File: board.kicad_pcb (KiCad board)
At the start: 2 copper layers, 96.3 x 46.3 mm, 38 parts, among them J0 Battery Pads, J1 PGRM, J2 Micro SD Slot, J3 USB_B_Micro, SW0 RESET, SW1 UP, SW2 DOWN, SW3 LEFT, SW4 RIGHT, SW5 BTN_A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

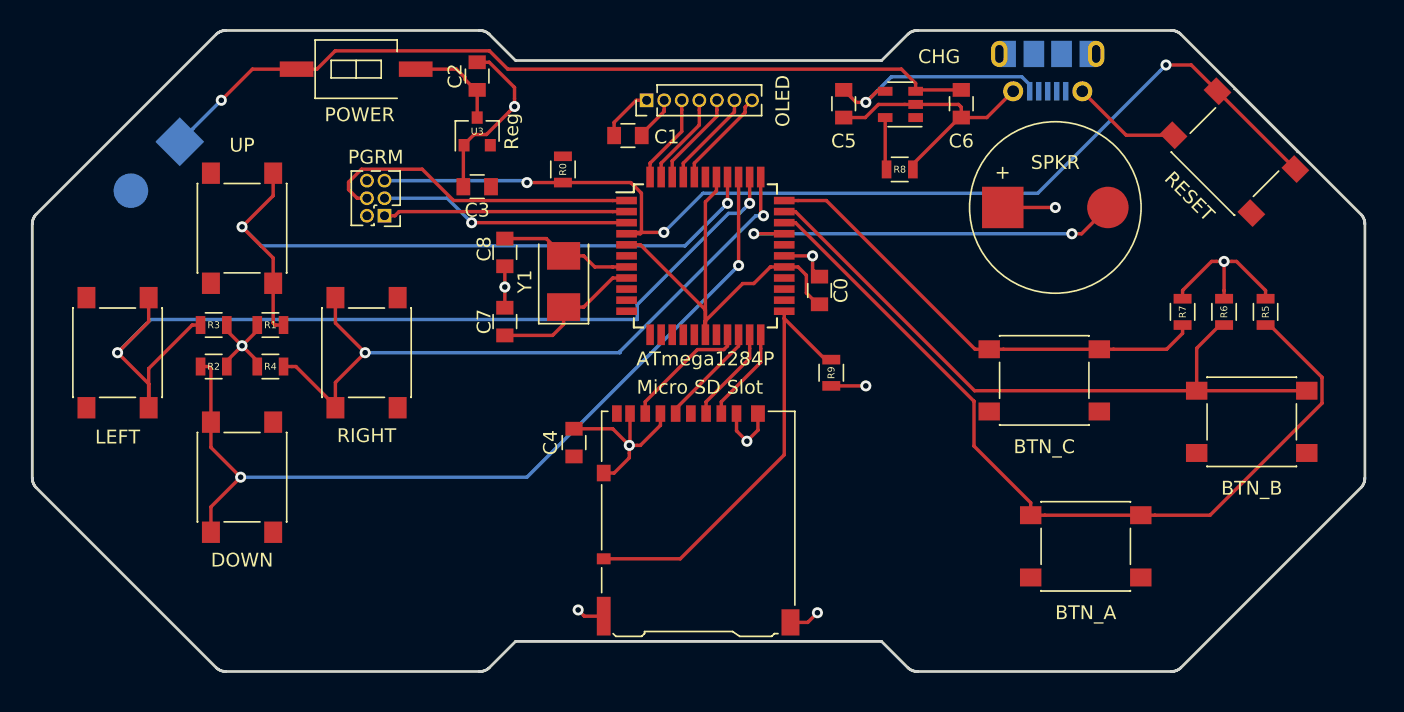
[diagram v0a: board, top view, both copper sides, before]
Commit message: reworked to be MCU agnostic
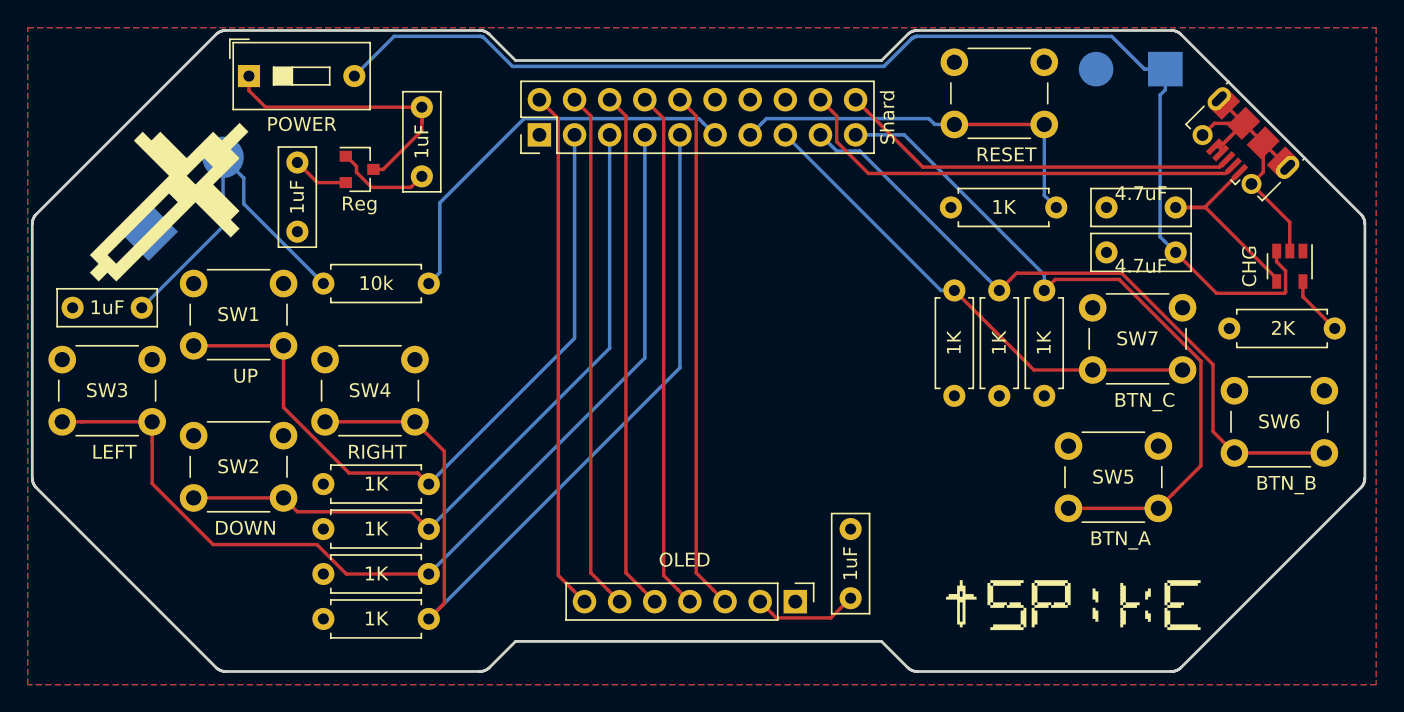
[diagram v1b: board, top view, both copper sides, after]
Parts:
- removed C0: 1uF, Capacitors_SMD:C_0805
- removed C7, C8: 22pF, Capacitors_SMD:C_0805
- removed J3: USB_B_Micro, Connectors_USB:USB_Micro-B_Molex-105017-0001
- removed U0: ATmega1284P, Housings_QFP:TQFP-44_10x10mm_Pitch0.8mm
- removed Y1: 16MHz, Crystals:Crystal_SMD_5032-2pin_5.0x3.2mm
- added LOGO: , LOGO, F.Cu at (168.5, 122.2)
- added SPIKE: , SPIKE, F.Cu at (114.0, 84.3)
- C1, C2, C3, C4, C5, C6: footprint Capacitors_SMD:C_0805 -> Capacitor_THT:C_Rect_L7.0mm_W2.5mm_P5.00mm
- J1: value PGRM -> Shard; footprint Pin_Headers:Pin_Header_Straight_2x03_Pitch1.27mm -> Connector_PinHeader_2.54mm:PinHeader_2x10_P2.54mm_Vertical
- J2: value Micro SD Slot -> USB-Micro; footprint Connectors_Card:Hirose_DM3AT-SF-PEJM5 -> Connector_USB:USB_Micro-B_Molex-105017-0001
- LS1: moved to B.Cu
- R0, R1, R2, R3, R4, R5, R6, R7, R8: footprint Resistors_SMD:R_0805 -> Resistor_THT:R_Axial_DIN0207_L6.3mm_D2.5mm_P7.62mm_Horizontal
- R9: value 1K -> 10k; footprint Resistors_SMD:R_0805 -> Resistor_THT:R_Axial_DIN0207_L6.3mm_D2.5mm_P7.62mm_Horizontal
- SW0, SW1, SW2, SW3, SW4, SW5, SW6, SW7: footprint Buttons_Switches_SMD:SW_SPST_PTS645 -> Button_Switch_THT:SW_PUSH_6mm
- SW8: footprint Buttons_Switches_SMD:SW_DIP_x1_W8.61mm_Slide_LowProfile -> Button_Switch_THT:SW_DIP_SPSTx01_Slide_9.78x4.72mm_W7.62mm_P2.54mm
- U1: footprint Custom Footprints:128x128_OLED -> Custom Footprints:128x128-OLED
- U2: footprint TO_SOT_Packages_SMD:SOT-23-5 -> Package_TO_SOT_SMD:SOT-23-5
- U3: footprint TO_SOT_Packages_SMD:SOT-23 -> Package_TO_SOT_SMD:SOT-23
- moved J0 65.2 mm to (182.2, 85.5), turned to 180 degrees
- moved LS1 61.8 mm to (111.2, 97.2), turned to 45 degrees
- moved J2 41.6 mm to (190.2, 91.0), turned to 135 degrees
- moved U1 37.8 mm to (158.0, 124.0), turned to 270 degrees
- moved C1 37.1 mm to (162.0, 123.8), turned to 90 degrees
- moved R8 33.5 mm to (197.0, 104.2), turned to 180 degrees
- moved C4 32.7 mm to (110.8, 102.8), turned to 180 degrees
- moved U2 30.5 mm to (193.8, 99.8), turned to 270 degrees
- moved R9 29.8 mm to (131.5, 101.0), turned to 180 degrees
- moved R0 28.2 mm to (169.2, 95.5), turned to 0 degrees
- moved C5 25.1 mm to (185.5, 95.5), turned to 180 degrees
- moved R3 23.8 mm to (131.5, 122.0), turned to 180 degrees
- moved R4 21.5 mm to (131.5, 125.2)
- moved SW0 21.3 mm to (169.5, 85.0), turned to 0 degrees
- moved R2 19.5 mm to (131.5, 118.8), turned to 180 degrees
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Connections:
- C4 pad 1: +3V3 -> Net-(C4-Pad1)
- J1 pad 1: MISO -> +3V3
- J1 pad 2: +3V3 -> D_CS
- J1 pad 3: SCK -> UP
- J1 pad 4: MOSI -> D_DC
- J1 pad 5: RESET -> DOWN
- J1 pad 6: GND -> D_RST
- J2 pad 1: GND -> CHARGE
- J2 pad 2: SD_CS -> D-
- J2 pad 3: SD_MOSI -> D+
- J2 pad 4: +3V3 -> GND
- J2 pad 5: SD_SCK -> GND
- LS1 pad 2: SND -> Net-(C4-Pad1)
- R9 pad 1: SD_DETECT -> SND
- R9 pad 2: GND -> Net-(C4-Pad1)
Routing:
- net GND: track 99.3 -> 31.7 mm, vias 11 -> 0
- net RESET: track 79.4 -> 28.3 mm, vias 3 -> 0
- net D-: track 0.00 -> 33.4 mm
- net SD_DETECT: track 31.2 -> 0.00 mm
- net D_SCK: track 6.50 -> 37.6 mm
- net D_MOSI: track 6.69 -> 37.6 mm
- net D_RST: track 6.89 -> 37.6 mm
- net D_DC: track 7.08 -> 37.6 mm
- net D_CS: track 7.28 -> 37.6 mm
- net D+: track 0.00 -> 29.1 mm
- net +BATT: track 60.8 -> 88.9 mm, vias 1 -> 0
- net Net-(C4-Pad1): track 0.00 -> 25.4 mm
- net +3V3: track 37.1 -> 11.7 mm
- net MOSI: track 23.6 -> 0.00 mm
- net SCK: track 18.2 -> 0.00 mm, vias 1 -> 0
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- added copper zone on F.Cu, net +3V3
- added copper zone on B.Cu, net GND

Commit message: added mounting holes
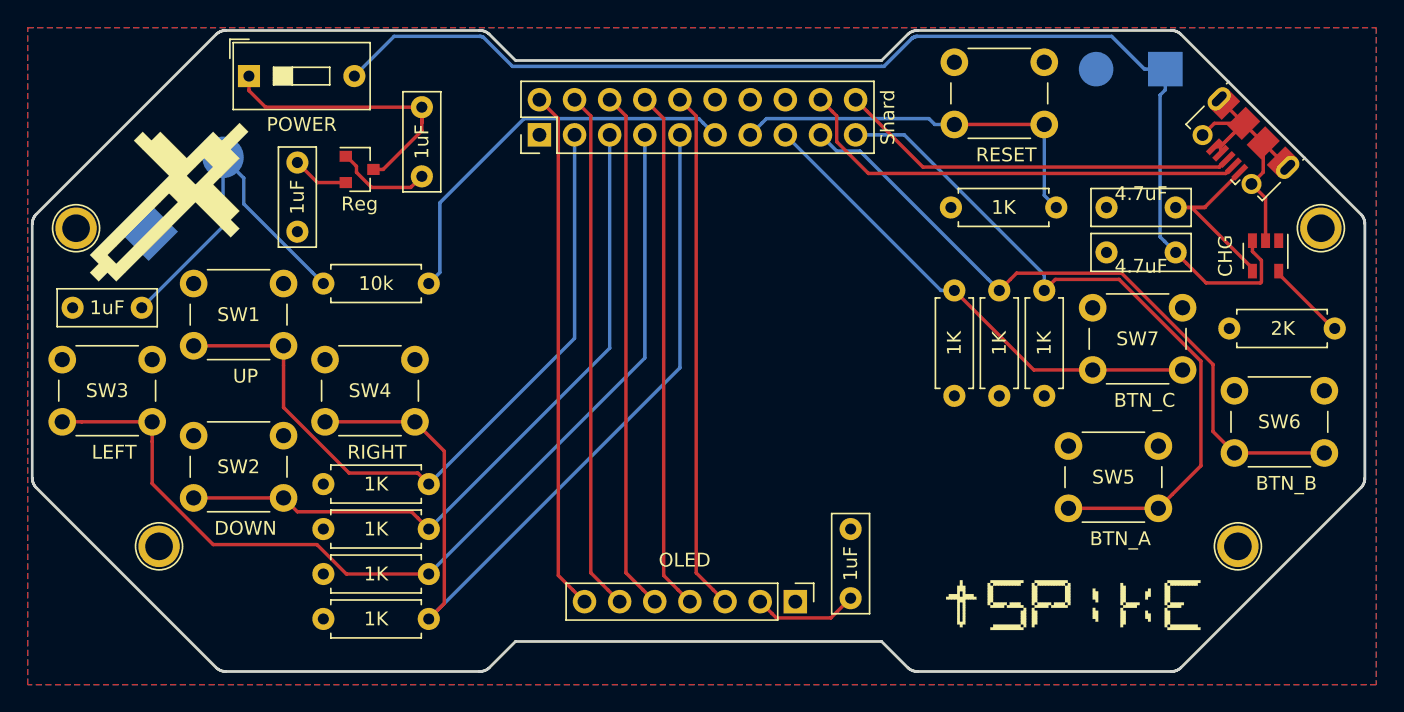
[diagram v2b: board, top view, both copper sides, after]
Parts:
- added REF**: TestPoint_Plated_Hole_D2.0mm, TestPoint:TestPoint_Plated_Hole_D2.0mm, F.Cu at (196.0, 97.0)
- added REF**: TestPoint_Plated_Hole_D2.0mm, TestPoint:TestPoint_Plated_Hole_D2.0mm, F.Cu at (106.0, 97.0)
- added REF**: TestPoint_Plated_Hole_D2.0mm, TestPoint:TestPoint_Plated_Hole_D2.0mm, F.Cu at (190.0, 120.0)
- added REF**: TestPoint_Plated_Hole_D2.0mm, TestPoint:TestPoint_Plated_Hole_D2.0mm, F.Cu at (112.0, 120.0)
- moved U2 1.90 mm to (192.0, 99.0)
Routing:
- net +BATT: track 88.9 -> 86.8 mm
- net Net-(R8-Pad1): track 4.35 -> 5.89 mm
- net GND: track 31.7 -> 30.2 mm
- net CHARGE: track 15.3 -> 14.3 mm
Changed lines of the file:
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@@
     (thickness 1.6)
     (drawings 102)
-    (tracks 182)
+    (tracks 185)
     (zones 0)
-    (modules 34)
+    (modules 38)
     (nets 25)
   )
@@
     (32 B.Adhes user hide)
     (33 F.Adhes user hide)
-    (34 B.Paste user)
+    (34 B.Paste user hide)
     (35 F.Paste user hide)
     (36 B.SilkS user)
@@
     (44 Edge.Cuts user)
     (45 Margin user hide)
-    (46 B.CrtYd user)
-    (47 F.CrtYd user)
-    (48 B.Fab user)
+    (46 B.CrtYd user hide)
+    (47 F.CrtYd user hide)
+    (48 B.Fab user hide)
     (49 F.Fab user hide)
   )
@@
       (outputformat 1)
       (mirror false)
-      (drillshape 1)
+      (drillshape 0)
       (scaleselection 1)
-      (outputdirectory ""))
+      (outputdirectory "/Users/mikewatts/Desktop/spike_gerbers/"))
   )
   (net 0 "")
@@
     (add_net SND)
     (add_net UP)
+  )
+  (module TestPoint:TestPoint_Plated_Hole_D2.0mm (layer F.Cu)
+    (at 196 97)
+    (descr "Plated Hole as test Point, diameter 2.0mm")
+    (tags "test point plated hole")
+    (attr virtual)
+    (fp_text reference REF** (at 0 -2.498) (layer F.Fab)
+      (effects (font (size 1 1) (thickness 0.15)))
+    )
+    (fp_text value TestPoint_Plated_Hole_D2.0mm (at 0 2.45) (layer F.Fab)
+      (effects (font (size 1 1) (thickness 0.15)))
+    )
+    (fp_text user %R (at 0 -2.5) (layer F.Fab)
+      (effects (font (size 1 1) (thickness 0.15)))
+    )
+    (fp_circle (center 0 0) (end 1.8 0) (layer F.CrtYd) (width 0.05))
+    (fp_circle (center 0 0) (end 0 -1.7) (layer F.SilkS) (width 0.12))
+    (pad 1 thru_hole circle (at 0 0) (size 3 3) (drill 2) (layers *.Cu *.Mask))
+  )
+  (module TestPoint:TestPoint_Plated_Hole_D2.0mm (layer F.Cu)
+    (at 106 97)
+    (descr "Plated Hole as test Point, diameter 2.0mm")
+    (tags "test point plated hole")
+    (attr virtual)
+    (fp_text reference REF** (at 0 -2.498) (layer F.Fab)
+      (effects (font (size 1 1) (thickness 0.15)))
+    )
+    (fp_text value TestPoint_Plated_Hole_D2.0mm (at 0 2.45) (layer F.Fab)
+      (effects (font (size 1 1) (thickness 0.15)))
+    )
+    (fp_circle (center 0 0) (end 0 -1.7) (layer F.SilkS) (width 0.12))
+    (fp_circle (center 0 0) (end 1.8 0) (layer F.CrtYd) (width 0.05))
+    (fp_text user %R (at 0 -2.5) (layer F.Fab)
+      (effects (font (size 1 1) (thickness 0.15)))
+    )
+    (pad 1 thru_hole circle (at 0 0) (size 3 3) (drill 2) (layers *.Cu *.Mask))
+  )
+  (module TestPoint:TestPoint_Plated_Hole_D2.0mm (layer F.Cu)
+    (at 190 120)
+    (descr "Plated Hole as test Point, diameter 2.0mm")
+    (tags "test point plated hole")
+    (attr virtual)
+    (fp_text reference REF** (at 0 -2.498) (layer F.Fab)
+      (effects (font (size 1 1) (thickness 0.15)))
+    )
+    (fp_text value TestPoint_Plated_Hole_D2.0mm (at 0 2.45) (layer F.Fab)
+      (effects (font (size 1 1) (thickness 0.15)))
+    )
+    (fp_text user %R (at 0 -2.5) (layer F.Fab)
+      (effects (font (size 1 1) (thickness 0.15)))
+    )
+    (fp_circle (center 0 0) (end 1.8 0) (layer F.CrtYd) (width 0.05))
+    (fp_circle (center 0 0) (end 0 -1.7) (layer F.SilkS) (width 0.12))
+    (pad 1 thru_hole circle (at 0 0) (size 3 3) (drill 2) (layers *.Cu *.Mask))
   )
   (module SPIKE (layer F.Cu)
@@
   )
   (module Package_TO_SOT_SMD:SOT-23-5 (layer F.Cu)
-    (at 193.75 99.75 270)
+    (at 192 99 270)
     (descr "5-pin SOT23 package")
     (tags SOT-23-5)
@@
     (pad 2 smd circle (at 2.5 0 180) (size 2.5 2.5) (layers B.Cu B.Paste B.Mask)
       (net 2 GND))
+  )
+  (module TestPoint:TestPoint_Plated_Hole_D2.0mm (layer F.Cu)
+    (at 112 120)
+    (descr "Plated Hole as test Point, diameter 2.0mm")
+    (tags "test point plated hole")
+    (attr virtual)
+    (fp_text reference REF** (at 0 -2.498) (layer F.Fab)
+      (effects (font (size 1 1) (thickness 0.15)))
+    )
+    (fp_text value TestPoint_Plated_Hole_D2.0mm (at 0 2.45) (layer F.Fab)
+      (effects (font (size 1 1) (thickness 0.15)))
+    )
+    (fp_circle (center 0 0) (end 0 -1.7) (layer F.SilkS) (width 0.12))
+    (fp_circle (center 0 0) (end 1.8 0) (layer F.CrtYd) (width 0.05))
+    (fp_text user %R (at 0 -2.5) (layer F.Fab)
+      (effects (font (size 1 1) (thickness 0.15)))
+    )
+    (pad 1 thru_hole circle (at 0 0) (size 3 3) (drill 2) (layers *.Cu *.Mask))
   )
   (gr_line (start 112.9 95) (end 108.8 99.1) (layer F.Mask) (width 1))
@@
   (segment (start 127.364997 94.049999) (end 130.200001 94.049999) (width 0.25) (layer F.Cu) (net 2))
   (segment (start 125.5 91.8) (end 125.55 91.8) (width 0.25) (layer F.Cu) (net 2))
-  (segment (start 193.75 96.568288) (end 193.75 98.65) (width 0.25) (layer F.Cu) (net 2))
-  (segment (start 190.983623 93.801911) (end 193.75 96.568288) (width 0.25) (layer F.Cu) (net 2))
   (segment (start 188.296617 89.417849) (end 187.448089 90.266377) (width 0.25) (layer F.Cu) (net 2))
   (segment (start 190.417938 89.417849) (end 188.296617 89.417849) (width 0.25) (layer F.Cu) (net 2))
@@
   (segment (start 188.650171 87.650082) (end 190.417938 89.417849) (width 0.25) (layer F.Cu) (net 2))
   (segment (start 191.832151 90.832062) (end 193.175654 92.175565) (width 0.25) (layer F.Cu) (net 2))
+  (segment (start 192 94.818288) (end 190.983623 93.801911) (width 0.25) (layer F.Cu) (net 2))
+  (segment (start 192 97.9) (end 192 94.818288) (width 0.25) (layer F.Cu) (net 2))
   (segment (start 131 89.3) (end 131 89) (width 0.25) (layer F.Cu) (net 3))
   (segment (start 127.5 92.75) (end 127.55 92.75) (width 0.25) (layer F.Cu) (net 3))
@@
   (segment (start 119.7 88.25) (end 118.5 87.05) (width 0.25) (layer F.Cu) (net 3))
   (segment (start 131 88.25) (end 119.7 88.25) (width 0.25) (layer F.Cu) (net 3))
-  (segment (start 186.63137 95.5) (end 185.5 95.5) (width 0.25) (layer F.Cu) (net 4))
-  (segment (start 192.8 100.645) (end 187.655 95.5) (width 0.25) (layer F.Cu) (net 4))
   (segment (start 187.655 95.5) (end 186.63137 95.5) (width 0.25) (layer F.Cu) (net 4))
-  (segment (start 192.8 100.85) (end 192.8 100.645) (width 0.25) (layer F.Cu) (net 4))
   (segment (start 187.588477 95.5) (end 185.5 95.5) (width 0.25) (layer F.Cu) (net 4))
   (segment (start 190.135095 92.953382) (end 187.588477 95.5) (width 0.25) (layer F.Cu) (net 4))
-  (segment (start 192.8 99.43) (end 192.8 98.65) (width 0.25) (layer F.Cu) (net 5))
-  (segment (start 193.450001 100.080001) (end 192.8 99.43) (width 0.25) (layer F.Cu) (net 5))
-  (segment (start 193.450001 101.640001) (end 193.450001 100.080001) (width 0.25) (layer F.Cu) (net 5))
-  (segment (start 193.385001 101.705001) (end 193.450001 101.640001) (width 0.25) (layer F.Cu) (net 5))
-  (segment (start 188.455001 101.705001) (end 193.385001 101.705001) (width 0.25) (layer F.Cu) (net 5))
-  (segment (start 185.5 98.75) (end 188.455001 101.705001) (width 0.25) (layer F.Cu) (net 5))
+  (segment (start 186.63137 95.5) (end 185.5 95.5) (width 0.25) (layer F.Cu) (net 4))
+  (segment (start 186.655 95.5) (end 186.63137 95.5) (width 0.25) (layer F.Cu) (net 4))
+  (segment (start 191.05 99.895) (end 186.655 95.5) (width 0.25) (layer F.Cu) (net 4))
+  (segment (start 191.05 100.1) (end 191.05 99.895) (width 0.25) (layer F.Cu) (net 4))
   (segment (start 184.374999 97.624999) (end 184.700001 97.950001) (width 0.25) (layer B.Cu) (net 5))
   (segment (start 184.374999 87.375001) (end 184.374999 97.624999) (width 0.25) (layer B.Cu) (net 5))
@@
   (segment (start 128.99219 83.12781) (end 126.12 86) (width 0.25) (layer B.Cu) (net 5))
   (segment (start 135.179837 83.12781) (end 128.99219 83.12781) (width 0.25) (layer B.Cu) (net 5))
+  (segment (start 186.299999 99.549999) (end 185.5 98.75) (width 0.25) (layer F.Cu) (net 5))
+  (segment (start 187.705001 100.955001) (end 186.299999 99.549999) (width 0.25) (layer F.Cu) (net 5))
+  (segment (start 191.635001 100.955001) (end 187.705001 100.955001) (width 0.25) (layer F.Cu) (net 5))
+  (segment (start 191.700001 100.890001) (end 191.635001 100.955001) (width 0.25) (layer F.Cu) (net 5))
+  (segment (start 191.700001 99.330001) (end 191.700001 100.890001) (width 0.25) (layer F.Cu) (net 5))
+  (segment (start 191.05 98.68) (end 191.700001 99.330001) (width 0.25) (layer F.Cu) (net 5))
+  (segment (start 191.05 97.9) (end 191.05 98.68) (width 0.25) (layer F.Cu) (net 5))
   (segment (start 176 94.63) (end 176 89.5) (width 0.25) (layer B.Cu) (net 6))
   (segment (start 176.87 95.5) (end 176 94.63) (width 0.25) (layer B.Cu) (net 6))
@@
   (segment (start 175.25 107.25) (end 169.5 101.5) (width 0.25) (layer F.Cu) (net 14))
   (segment (start 179.5 107.25) (end 175.25 107.25) (width 0.25) (layer F.Cu) (net 14))
-  (segment (start 194.7 101.95) (end 197 104.25) (width 0.25) (layer F.Cu) (net 15))
-  (segment (start 194.7 100.85) (end 194.7 101.95) (width 0.25) (layer F.Cu) (net 15))
+  (segment (start 196.895 104.25) (end 197 104.25) (width 0.25) (layer F.Cu) (net 15))
+  (segment (start 192.95 100.305) (end 196.895 104.25) (width 0.25) (layer F.Cu) (net 15))
+  (segment (start 192.95 100.1) (end 192.95 100.305) (width 0.25) (layer F.Cu) (net 15))
   (segment (start 143.215001 121.915001) (end 144.450001 123.150001) (width 0.25) (layer F.Cu) (net 16))
   (segment (start 144.450001 123.150001) (end 145.3 124) (width 0.25) (layer F.Cu) (net 16))
@@
   (segment (start 189.127469 93.04177) (end 163.29177 93.04177) (width 0.25) (layer F.Cu) (net 24))
   (segment (start 189.675476 92.493763) (end 189.127469 93.04177) (width 0.25) (layer F.Cu) (net 24))
-  (zone (net 2) (net_name GND) (layer B.Cu) (hatch edge 0.508)
+  (zone (net 1) (net_name +3V3) (layer F.Cu) (hatch edge 0.508)
     (connect_pads (clearance 0.508))
     (min_thickness 0.254)
@@
     )
   )
-  (zone (net 1) (net_name +3V3) (layer F.Cu) (hatch edge 0.508)
+  (zone (net 2) (net_name GND) (layer B.Cu) (hatch edge 0.508)
     (connect_pads (clearance 0.508))
     (min_thickness 0.254)
